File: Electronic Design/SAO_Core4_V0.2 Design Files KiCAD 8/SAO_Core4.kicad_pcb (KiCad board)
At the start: 2 copper layers, 50.8 x 63.5 mm, 92 parts, among them Q1 MMBT4403LT1G, Q13 MMBT4403LT1G, Q14 MMBT4401LT1G, Q17 MMBT4403LT1G, Q18 MMBT4401LT1G, Q2 MMBT4401LT1G, Q21 Q_NMOS_DGS_AO3400A, Q22 SL3401A, Q3 MMBT4403LT1G, Q4 MMBT4401LT1G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

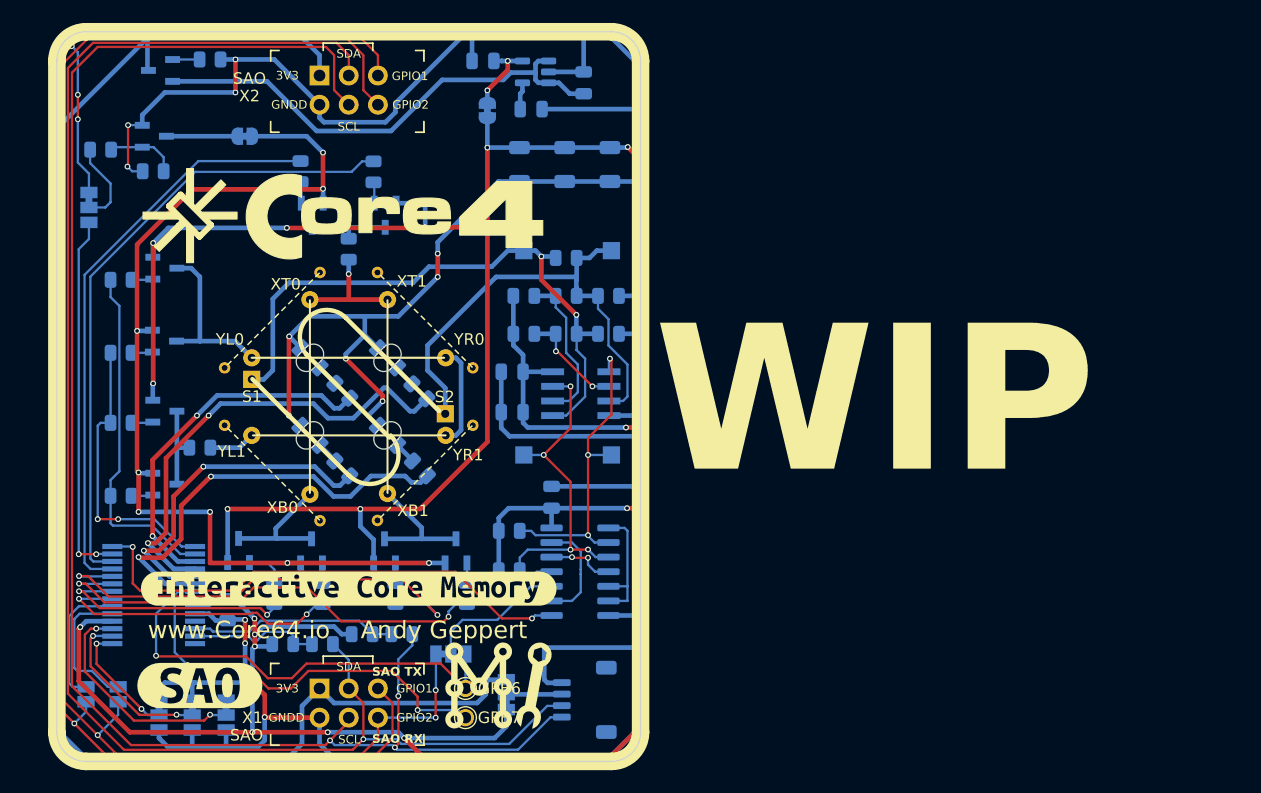
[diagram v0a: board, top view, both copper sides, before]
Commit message: Shrink V0.2 PCB size
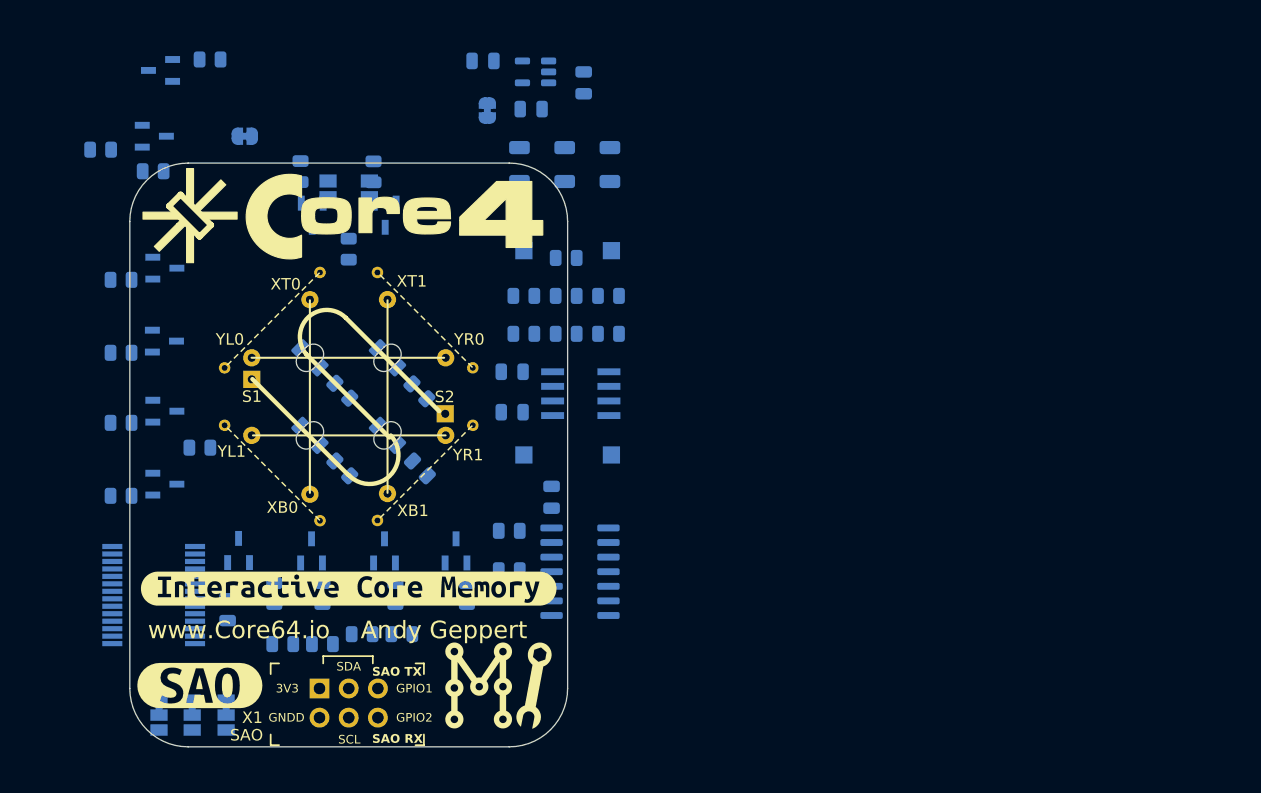
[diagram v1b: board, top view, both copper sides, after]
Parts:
- removed JP21: V_SEL, Jumper:SolderJumper-3_P1.3mm_Bridged12_Pad1.0x1.5mm
- removed JP22: INTA, Jumper:SolderJumper-2_P1.3mm_Open_Pad1.0x1.5mm
- removed JP23: INTB, Jumper:SolderJumper-2_P1.3mm_Open_Pad1.0x1.5mm
- removed JP24, JP25: CM_SNS_SEL, Jumper:SolderJumper-3_P1.3mm_Bridged12_Pad1.0x1.5mm
- removed TP6: GPB6, Andy_Footprint_Library:TestPoint_THTPad_D1.5mm_Drill1.0mm
- removed TP7: GPB7, Andy_Footprint_Library:TestPoint_THTPad_D1.5mm_Drill1.0mm
- removed X2: SAO_conn_SFH11-NBPC-D03-ST-BK, Andy_Footprint_Library:Badgelife-SAOv169-BADGE-2x3
- removed X3: QWIIC, Connector_JST:JST_SH_SM04B-SRSS-TB_1x04-1MP_P1.00mm_Horizontal
- removed kibuzzard-64178E7C: G***, kibuzzard-64178E7C
- added SW1: Button Edge EVQ-P7J01P, Andy_Footprint_Library:SMD4_SW_EVQP7J_PAN, B.Cu at (107.5, 107.8)
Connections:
- R13 pad 2: /CMDQ-7P9N -> /CMDQ-7P
- R14 pad 2: /CMDQ-7N9P -> /CMDQ-7N
- R17 pad 2: /CMDQ-7N9P -> /CMDQ-9P
- R18 pad 2: /CMDQ-7P9N -> /CMDQ-9N
- U10 pad 10: /CM_SNS_PLS -> /GPIO2
- U10 pad 11: /CM_SNS_PLS -> /GPIO2
- U11 pad 1: /CMDQ-7N9P -> /CMDQ-7N
- U11 pad 19: Net-(JP23-B) -> unconnected-(U11-INTB-Pad19)
- U11 pad 2: /CMDQ-7P9N -> /CMDQ-7P
- U11 pad 20: Net-(JP22-B) -> unconnected-(U11-INTA-Pad20)
- U11 pad 27: /SPARE_GPA6 -> /CM_EN
- U11 pad 7: /SPARE_GPB6 -> /CMDQ-9N
- U11 pad 8: /SPARE_GPB7 -> /CMDQ-9P
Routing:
- net 3V3: track 327.6 -> 0.00 mm, vias 17 -> 0
- net GND: track 307.5 -> 0.00 mm, vias 14 -> 0
- net /SCL: track 141.8 -> 0.00 mm, vias 3 -> 0
- net /GPIO1: track 139.7 -> 0.00 mm, vias 4 -> 0
- net /SDA: track 138.3 -> 0.00 mm, vias 1 -> 0
- net /GPIO2: track 133.8 -> 0.00 mm, vias 3 -> 0
- net VIN: track 129.7 -> 0.00 mm
- net GMEM: track 87.5 -> 0.00 mm, vias 8 -> 0
- net /CMDQ-3P: track 55.3 -> 0.00 mm
- net /CM_SENSE_1_IN: track 54.0 -> 0.00 mm, vias 2 -> 0
- net /CMDQ-3N: track 50.6 -> 0.00 mm
- net /CM_SNS_RST: track 44.2 -> 0.00 mm, vias 2 -> 0
- net Net-(Q22-S): track 42.7 -> 0.00 mm
- net /CM_SENSE_2_IN: track 42.1 -> 0.00 mm
- net /LED_2: track 41.0 -> 0.00 mm, vias 2 -> 0
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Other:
- board size 50.8 x 63.5 mm -> 38.1 x 50.8 mm
- board text removed: "3V3"
- board text removed: "GPB6"
- board text removed: "GPB7"
- board text removed: "VIN"
- board text removed: "WIP"

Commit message: HWV0.2: Create WIP schematics pdf and renders
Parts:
- moved R5 105.2 mm to (107.6, 211.5)
- moved SW1 105.2 mm to (105.5, 213.0)
- moved Q5 105.2 mm to (108.6, 215.3)
- moved Q6 105.2 mm to (102.3, 215.3)
- moved R21 105.2 mm to (105.5, 218.2)
- moved R6 105.2 mm to (101.3, 211.5)
- moved U11 100.8 mm to (67.6, 241.3)
- moved Q18 96.2 mm to (70.9, 227.4)
- moved R13 96.2 mm to (67.1, 209.7)
- moved R17 96.2 mm to (67.1, 222.1)
- moved R18 96.2 mm to (67.1, 228.5)
- moved R14 96.2 mm to (67.1, 216.0)
- moved Q13 96.2 mm to (70.9, 208.6)
- moved Q14 96.2 mm to (70.9, 215.0)
- moved Q17 96.2 mm to (70.9, 221.1)
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
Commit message: Add SAo Core4 V0.2 files, demo code update
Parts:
- removed Q22: SL3401A, digikey-footprints:SOT-23-3
- removed R32, R33: 0, Resistor_SMD:R_0805_2012Metric
- removed R44: 4K7, Resistor_SMD:R_0805_2012Metric
- removed TP20: S1 IN, TestPoint:TestPoint_Pad_1.5x1.5mm
- removed TP21: S2 IN, TestPoint:TestPoint_Pad_1.5x1.5mm
- removed TP22: S2 OUT, TestPoint:TestPoint_Pad_1.5x1.5mm
- removed TP23: S1 OUT, TestPoint:TestPoint_Pad_1.5x1.5mm
- removed kibuzzard-6417AF30: G***, kibuzzard-6417AF30
- removed kibuzzard-66C5FD34: G***, kibuzzard-66C5FD34
- removed kibuzzard-66C5FD67: G***, kibuzzard-66C5FD67
- added J1: V+ALT, Connector_PinSocket_1.27mm:PinSocket_1x01_P1.27mm_Vertical, B.Cu at (122.5, 155.3)
- added JP1: VSEL, Jumper:SolderJumper-3_P1.3mm_Bridged12_Pad1.0x1.5mm, B.Cu at (116.5, 155.1)
- R21, R7: value 8R2-5% -> 6R8-5%
- R27: value 4K7 -> 10K
- R30, R31, R54, R55: value 1K2 -> 10K
- X1: footprint Andy_Footprint_Library:Badgelife-SAOv169-BADGE-2x3 -> Andy_Footprint_Library:Badgelife-SAOv169-BADGE-2x3-Edge-Connect-no-front-text
- moved U10 129.8 mm to (96.6, 109.8), turned to -90 degrees
- moved C19 121.8 mm to (90.8, 113.3), turned to -90 degrees
- moved C18 111.4 mm to (117.9, 107.9), turned to 90 degrees
- moved C17 107.6 mm to (120.1, 107.9), turned to 90 degrees
- moved U9 103.0 mm to (121.5, 115.2)
- moved U11 102.7 mm to (93.7, 142.0)
- moved R6 102.3 mm to (104.5, 109.2)
- moved Q6 102.3 mm to (105.4, 113.0)
- moved R5 102.2 mm to (108.8, 109.2)
- moved Q5 102.2 mm to (109.7, 113.0)
- moved R21 101.4 mm to (107.5, 116.8)
- moved Q18 98.0 mm to (95.6, 132.6)
- moved R18 98.0 mm to (91.8, 133.7)
- moved R7 96.5 mm to (101.7, 131.8), turned to -90 degrees
- moved Q17 96.2 mm to (95.6, 128.1)
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- renumbered R60 to R61, R61 to R62, R62 to R63, R63 to R64
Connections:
- net /GPIO2 renamed /CM_SNS_PLS
- CM1 pad 1: Net-(CM1-XT0) -> /XT0,1
- CM1 pad 2: Net-(CM1-XT0) -> /XT0,1
- Q5 pad 3: /XT0,1 -> Net-(Q5-C)
- Q6 pad 3: /XT0,1 -> Net-(Q5-C)
- R21 pad 1: /XT0,1 -> Net-(Q5-C)
- R21 pad 2: Net-(CM1-XT0) -> /XT0,1
- R30 pad 2: /I2C_SCL -> /SCL
- R31 pad 2: /I2C_SDA -> /SDA
- SW1 pad 1: unconnected-(SW1-Pad1) -> /GPIO1
- SW1 pad 2: unconnected-(SW1-Pad2) -> /GPIO1
- SW1 pad 3: unconnected-(SW1-Pad3) -> GND
- SW1 pad 4: unconnected-(SW1-Pad4) -> GND
- U11 pad 1: /CMDQ-7N -> /LED_1
- U11 pad 12: /I2C_SCL -> /SCL
- U11 pad 13: /I2C_SDA -> /SDA
- U11 pad 2: /CMDQ-7P -> /LED_2
- U11 pad 3: /LED_1 -> /LED_3
- U11 pad 4: /LED_2 -> /LED_4
- U11 pad 5: /LED_3 -> /CMDQ-7N
- U11 pad 6: /LED_4 -> /CMDQ-7P
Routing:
- net GND: track 0.00 -> 223.7 mm, vias 0 -> 7
- net 3V3: track 0.00 -> 197.6 mm, vias 0 -> 19
- net /CM_SNS_PLS: track 0.00 -> 76.7 mm, vias 0 -> 2
- net GMEM: track 0.00 -> 69.8 mm, vias 0 -> 6
- net /CM_SENSE_1_IN: track 0.00 -> 53.8 mm, vias 0 -> 4
- net /CMDQ-3P: track 0.00 -> 52.3 mm
- net /CMDQ-3N: track 0.00 -> 47.2 mm
- net /CM_SNS_RST: track 0.00 -> 39.7 mm, vias 0 -> 4
- net /CM_EN: track 0.00 -> 38.4 mm, vias 0 -> 2
- net /CA_SENSE_1_OUT: track 0.00 -> 37.1 mm, vias 0 -> 2
- net /CA_SENSE_2_OUT: track 0.00 -> 36.2 mm, vias 0 -> 2
- net /LED_2: track 0.00 -> 34.8 mm, vias 0 -> 2
- net /LED_4: track 0.00 -> 31.5 mm, vias 0 -> 2
- net /CMDQ-2N: track 0.00 -> 29.5 mm, vias 0 -> 2
- net /GPIO1: track 0.00 -> 28.8 mm, vias 0 -> 2
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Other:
- outline, holes or cut-outs redrawn
- board text added: "+"
- board text added: "-"
- board text added: "0x20-27"
- board text added: "0x27"
- board text added: "3V3"
- board text added: "435171014816"
- board text added: "A+"
- board text added: "A2 A1 A0"
- board text added: "EN"
- board text added: "LS38J2F Button Fix"
- board text added: "R-667996"
- board text added: "V0.2"
- board text removed: "+A2+A1+A0"
- board text removed: "0x20-27 (default 27)"
- board text removed: "2GPIO1"
- board text removed: "3V3 CUR MON"
- board text removed: "CM_EN"
- board text removed: "GMEM CUR MON"
- board text removed: "GPA6"
- board text removed: "GPIO1"
- board text removed: "LOGIC LEVELS 3.3V"
- board text removed: "OUT"
- board text removed: "PCB: 612-001 REV: 0.1 PCBA: 612-000"
- board text removed: "S2>IN<S1"
- board text removed: "SAO Contest Size 2x1.5inch"
- board text removed: "SAO RX"
- board text removed: "SAO TX"
- board text removed: "SENSE"
